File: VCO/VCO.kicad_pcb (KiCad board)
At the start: 2 copper layers, 45 parts, among them J1 Input, J2 Power, J3 Output, J4 PW, Q1 BC807, Q2 BC807, Q3 BC807, U1 LM324A, U2 LM324A

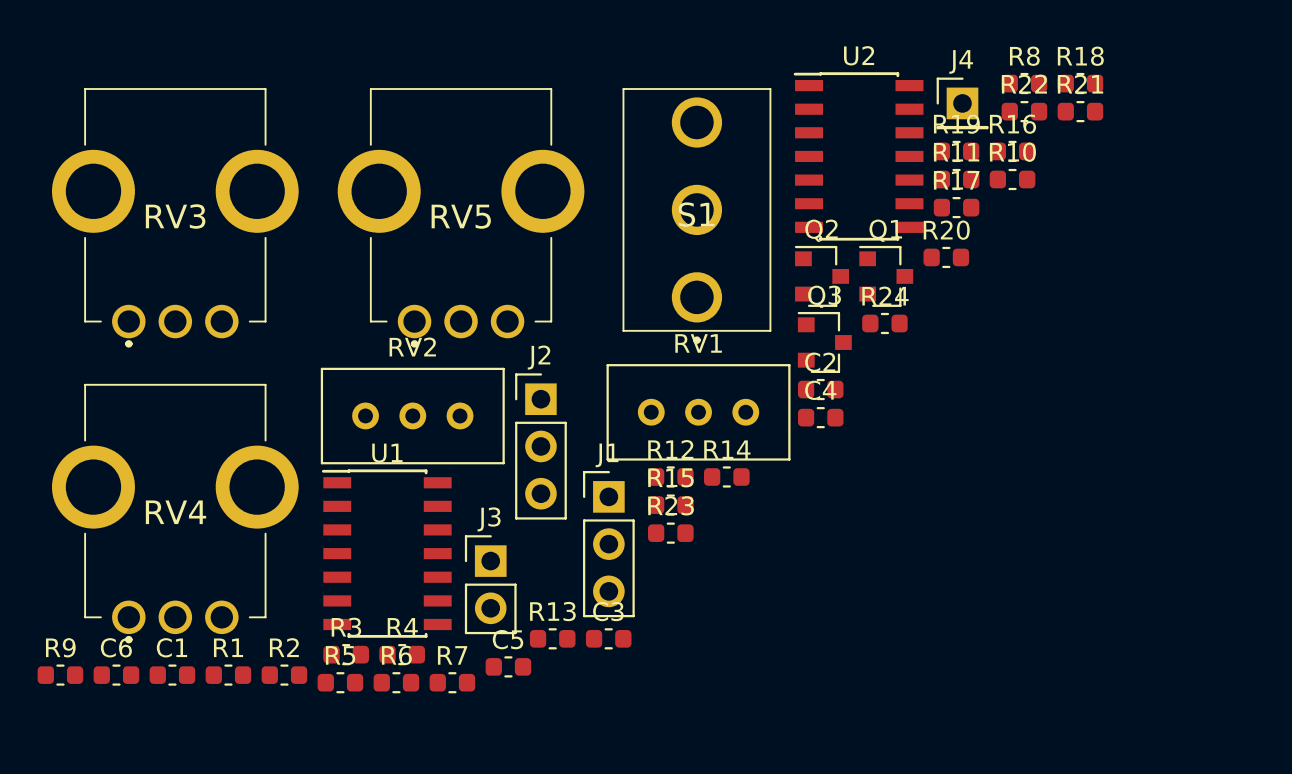
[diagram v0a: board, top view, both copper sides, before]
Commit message: Изменены библиотеки. Добавлинны библиотеки примененные в проекте локально. Добавленны заготовки для печатных плат. Добавленны 3D модели компоненток.
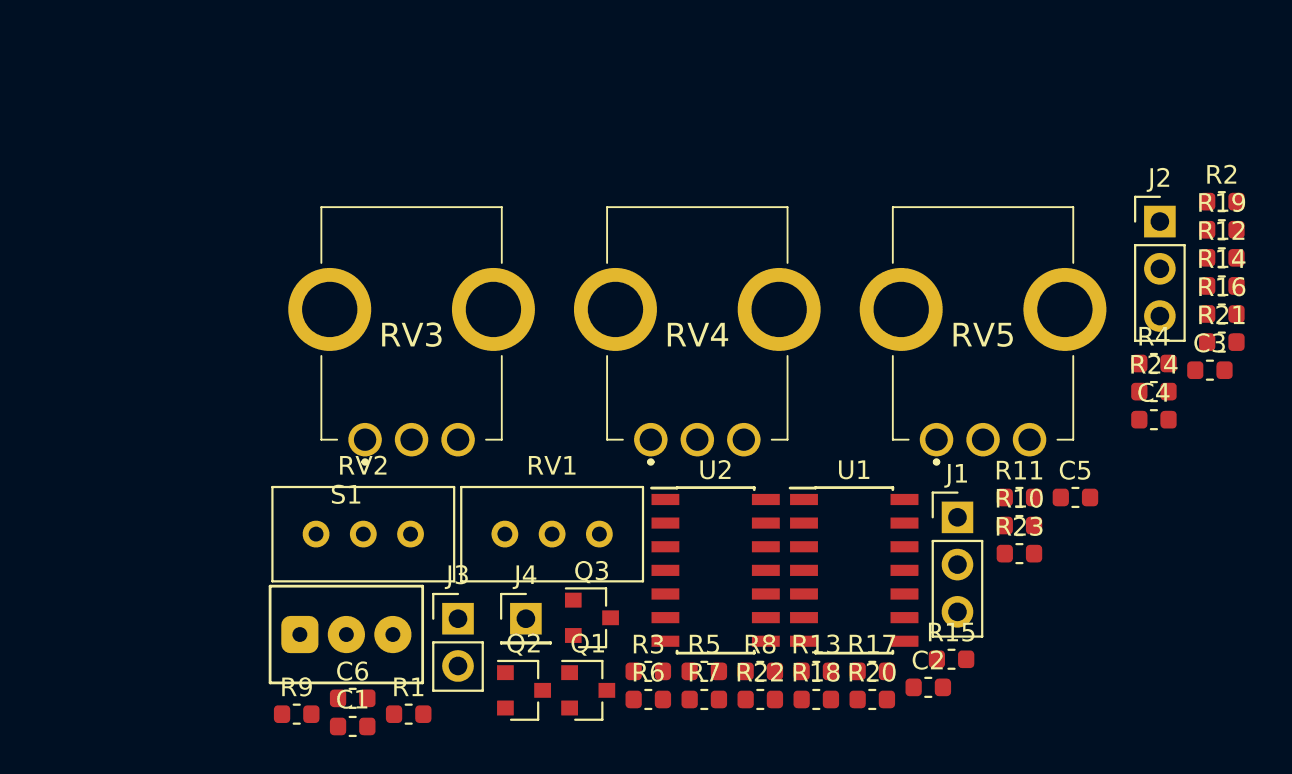
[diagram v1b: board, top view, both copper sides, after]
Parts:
- C1, C2, C3, C4, C5, C6: footprint Capacitor_SMD:C_0603_1608Metric -> footprint:c0603
- J1, J2: footprint Connector_PinHeader_2.54mm:PinHeader_1x03_P2.54mm_Vertical -> footprint:pls1x03
- J3: footprint Connector_PinHeader_2.54mm:PinHeader_1x02_P2.54mm_Vertical -> footprint:pls1x02
- J4: footprint Connector_PinHeader_2.54mm:PinHeader_1x01_P2.54mm_Vertical -> footprint:pls1x01
- Q1, Q2, Q3: footprint Package_TO_SOT_SMD:SOT-23 -> footprint:SOT-23
- R1, R10, R11, R12, R13, R14, R15, R16, R17, R18, R19, R2, R20, R21, R22, R23, R24, R3, R4, R5, R6, R7, R8, R9: footprint Resistor_SMD:R_0603_1608Metric -> footprint:r0603
- RV1, RV2: footprint Potentiometer_THT:Potentiometer_Bourns_3296W_Vertical -> footprint:w3296w
- RV3, RV4, RV5: footprint R0409N:PTV09A4020FB103 -> footprint:PTV09A4020FB103
- S1: footprint M2013SS1W03:M2018SD3G03 -> footprint:smts-102-2a2
- U1, U2: footprint Package_SO:SOIC-14_3.9x8.7mm_P1.27mm -> footprint:soic-14
- moved R2 56.5 mm to (178.2, 71.9)
- moved R4 43.3 mm to (174.6, 80.6)
- moved J4 36.3 mm to (140.8, 94.3)
- moved R18 36.0 mm to (156.4, 98.6)
- moved C3 35.4 mm to (177.6, 80.9)
- moved R22 34.6 mm to (153.4, 98.6)
- moved R8 34.6 mm to (153.4, 97.1)
- moved J2 34.6 mm to (174.9, 72.9)
- moved R12 31.9 mm to (178.2, 74.9)
- moved C5 31.8 mm to (170.4, 87.8)
- moved RV4 29.6 mm to (150.0, 79.1)
- moved S1 29.6 mm to (131.2, 95.1)
- moved RV5 28.8 mm to (165.4, 79.1)
- moved R14 28.5 mm to (178.2, 76.4)
- moved Q2 27.4 mm to (140.7, 98.1)
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
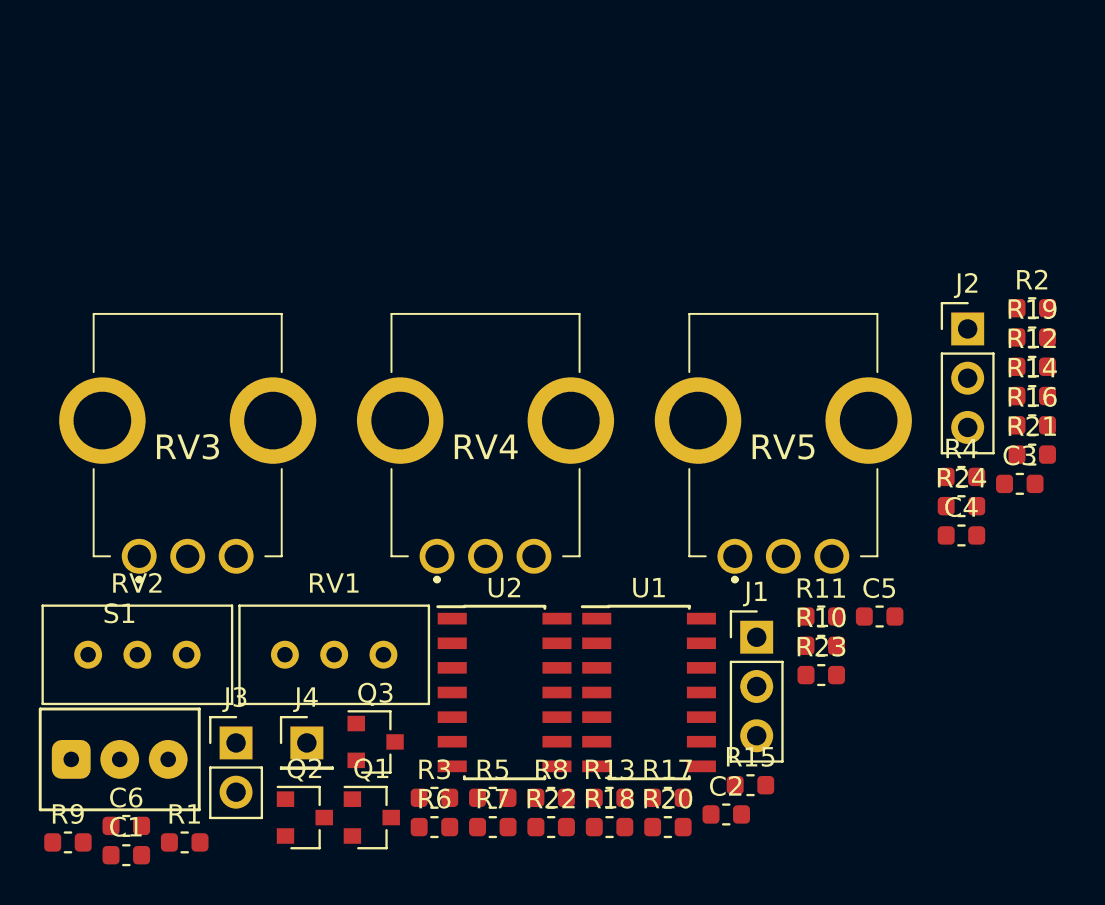
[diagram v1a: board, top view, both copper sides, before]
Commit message: Исправленну ошибки в схемах. Полностью локальные библиотеки и 3D модели.
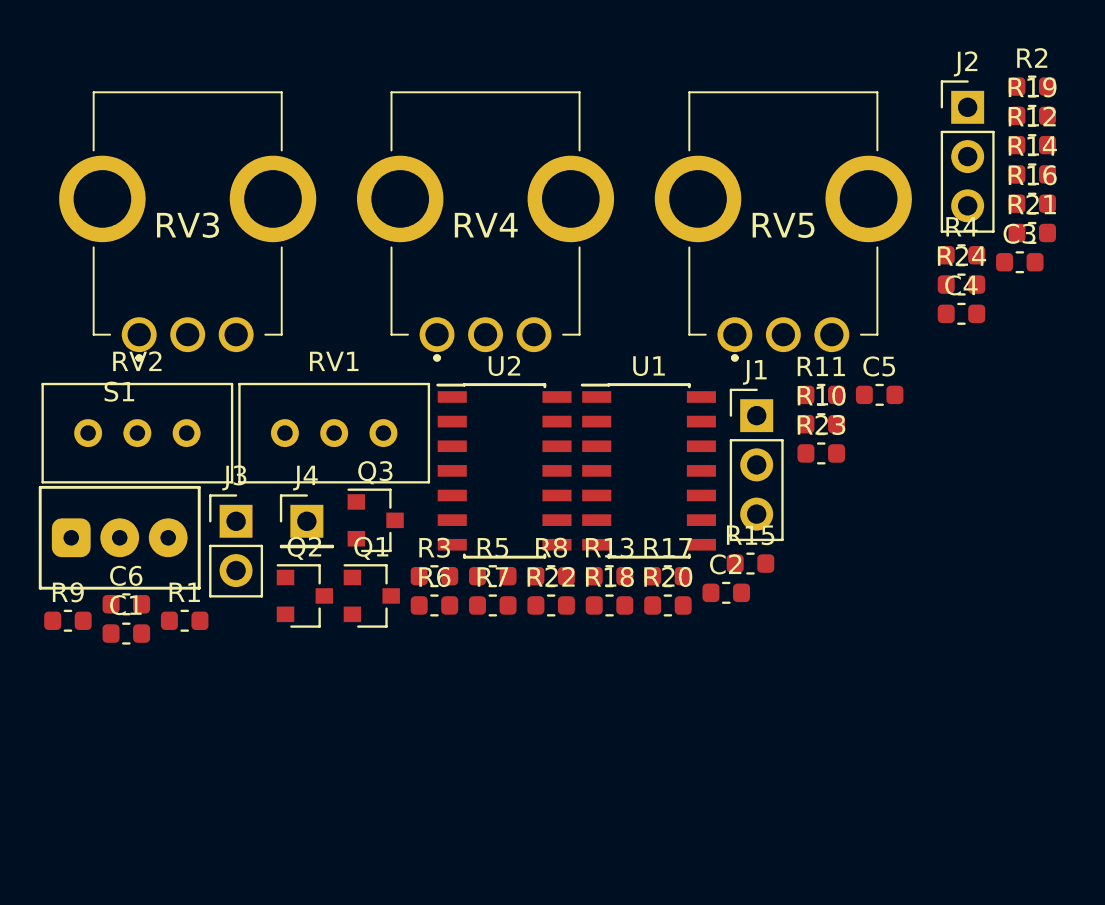
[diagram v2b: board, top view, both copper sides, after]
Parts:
- S1: footprint footprint:smts-102-2a2 -> footprint:smts
- moved C1 11.4 mm to (131.5, 88.7)
- moved C3 11.4 mm to (177.6, 69.5)
- moved C5 11.4 mm to (170.4, 76.3)
- moved C6 11.4 mm to (131.5, 87.1)
- moved J2 11.4 mm to (174.9, 61.5)
- moved Q3 11.4 mm to (144.4, 82.8)
- moved R11 11.4 mm to (167.4, 76.3)
- moved R15 11.4 mm to (163.7, 85.0)
- moved R16 11.4 mm to (178.2, 66.5)
- moved R18 11.4 mm to (156.4, 87.2)
- moved R20 11.4 mm to (159.4, 87.2)
- moved R22 11.4 mm to (153.4, 87.2)
- moved R24 11.4 mm to (174.6, 70.7)
- moved R4 11.4 mm to (174.6, 69.1)
- moved R6 11.4 mm to (147.4, 87.2)
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
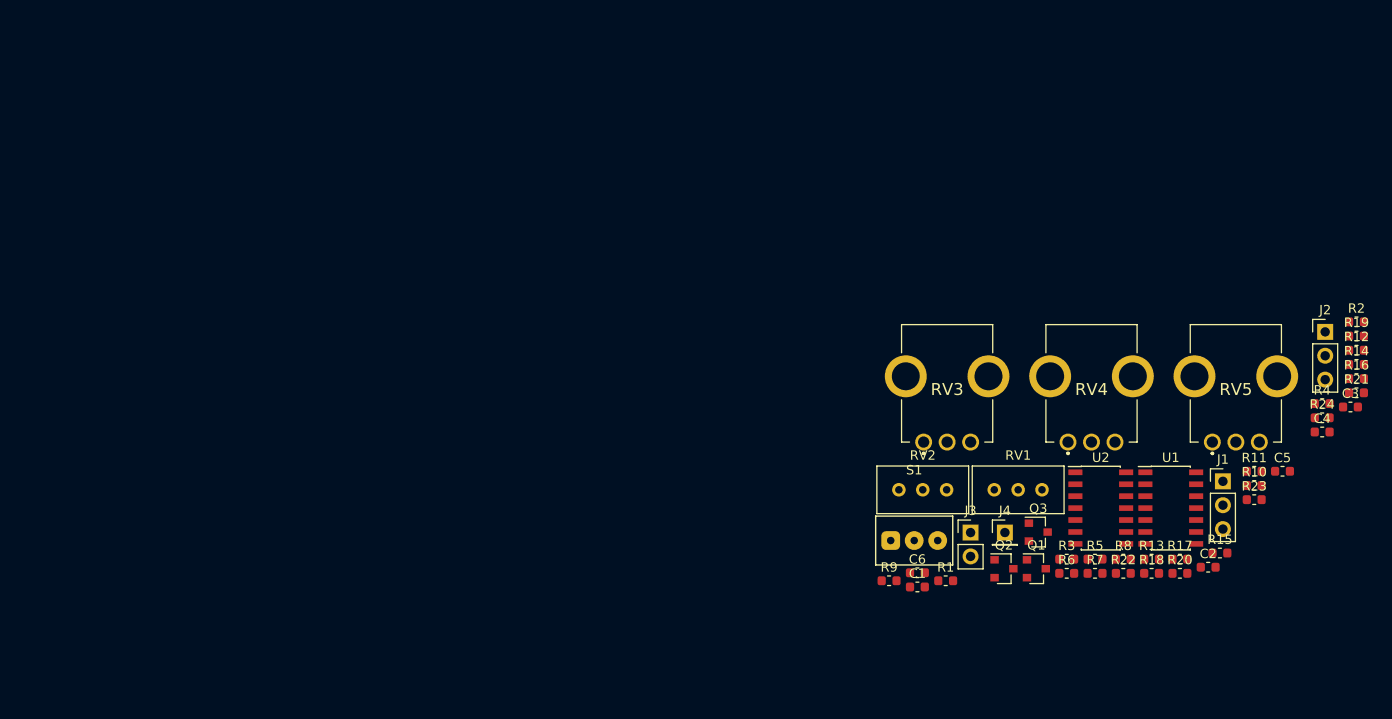
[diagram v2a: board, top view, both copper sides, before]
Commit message: ADD PCB module VCO. ADD folder MOTHEBORD.
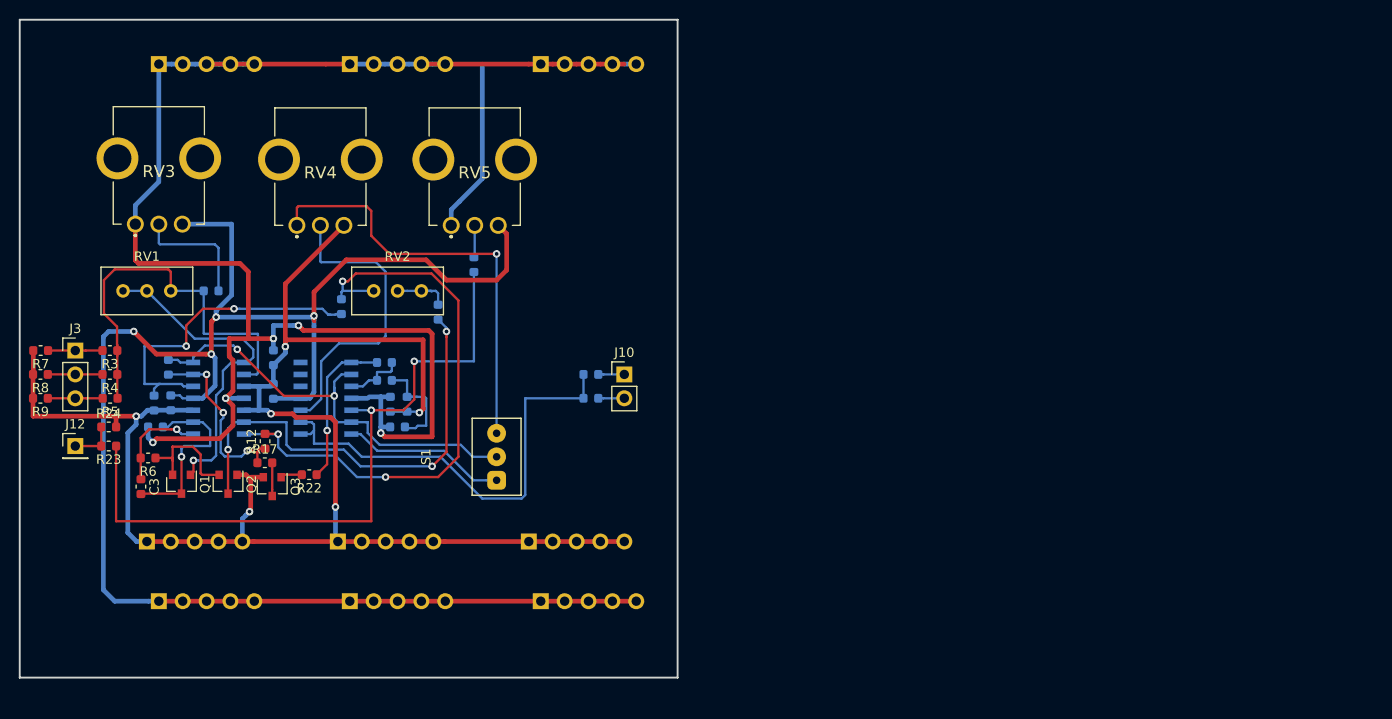
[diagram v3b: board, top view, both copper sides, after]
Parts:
- added J10: Output, footprint:pls1x02, F.Cu at (100.3, 66.0)
- added J11: Conn_01x05_Male, footprint:pls1x05, B.Cu at (91.4, 90.2)
- added J12: PW, footprint:pls1x01, F.Cu at (41.9, 73.7)
- added J5: Conn_01x05_Male, footprint:pls1x05, B.Cu at (49.5, 83.8)
- added J6: Conn_01x05_Male, footprint:pls1x05, B.Cu at (69.8, 83.8)
- added J7: Conn_01x05_Male, footprint:pls1x05, B.Cu at (90.2, 83.8)
- added J8: Conn_01x05_Male, footprint:pls1x05, B.Cu at (50.8, 90.2)
- added J9: Conn_01x05_Male, footprint:pls1x05, B.Cu at (71.1, 90.2)
- C1, C2, C4, C5, C6, R1, R10, R11, R13, R14, R15, R16, R18, R19, R2, R20, R21, U1, U2: moved to B.Cu
- J1: value Input -> Conn_01x05_Male; footprint footprint:pls1x03 -> footprint:pls1x05; moved to B.Cu
- J2: value Power -> Conn_01x05_Male; footprint footprint:pls1x03 -> footprint:pls1x05; moved to B.Cu
- J3: value Output -> Input; footprint footprint:pls1x02 -> footprint:pls1x03
- J4: value PW -> Conn_01x05_Male; footprint footprint:pls1x01 -> footprint:pls1x05; moved to B.Cu
- moved R24 129.1 mm to (45.5, 71.6)
- moved R4 129.0 mm to (45.6, 66.0), turned to 180 degrees
- moved C3 129.0 mm to (48.9, 78.0), turned to 270 degrees
- moved R23 122.0 mm to (45.5, 73.7), turned to 180 degrees
- moved C5 118.5 mm to (52.1, 69.1), turned to 270 degrees
- moved R8 116.9 mm to (38.2, 66.0), turned to 180 degrees
- moved R12 116.5 mm to (62.1, 73.2), turned to 90 degrees
- moved R7 114.7 mm to (38.2, 63.5), turned to 180 degrees
- moved R15 114.5 mm to (50.3, 69.1), turned to 270 degrees
- moved R10 112.9 mm to (56.4, 57.1)
- moved C4 111.7 mm to (63.0, 67.8), turned to 90 degrees
- moved R14 108.2 mm to (70.2, 58.8), turned to 90 degrees
- moved R5 106.2 mm to (45.6, 68.6), turned to 180 degrees
- moved R3 104.2 mm to (45.6, 63.5), turned to 180 degrees
- moved R19 103.5 mm to (74.8, 64.8)
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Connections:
- J1 pad 1: /IN_1 -> +5V
- J1 pad 2: /IN_2 -> +5V
- J1 pad 3: /IN_3 -> +5V
- J2 pad 2: GNDREF -> +5V
- J2 pad 3: -5V -> +5V
- J3 pad 1: Net-(J3-Pad1) -> /IN_1
- J3 pad 2: Net-(J3-Pad2) -> /IN_2
- J4 pad 1: /PW -> +5V
- R11 pad 1: Net-(J3-Pad1) -> Net-(J10-Pad1)
- R13 pad 1: Net-(J3-Pad2) -> Net-(J10-Pad2)
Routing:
- net +5V: track 0.00 -> 225.1 mm, vias 0 -> 5
- net -5V: track 0.00 -> 217.5 mm, vias 0 -> 4
- net GNDREF: track 0.00 -> 210.6 mm, vias 0 -> 6
- net Net-(R21-Pad1): track 0.00 -> 74.0 mm, vias 0 -> 2
- net Net-(R12-Pad2): track 0.00 -> 64.4 mm, vias 0 -> 3
- net Net-(R11-Pad2): track 0.00 -> 49.2 mm
- net Net-(Q2-Pad3): track 0.00 -> 48.9 mm, vias 0 -> 3
- net Net-(C6-Pad1): track 0.00 -> 47.6 mm, vias 0 -> 2
- net Net-(RV4-Pad1): track 0.00 -> 46.1 mm, vias 0 -> 1
- net Net-(R10-Pad1): track 0.00 -> 42.4 mm
- net Net-(R14-Pad1): track 0.00 -> 35.3 mm, vias 0 -> 2
- net Net-(Q1-Pad1): track 0.00 -> 34.7 mm, vias 0 -> 1
- net Net-(RV4-Pad2): track 0.00 -> 32.8 mm
- net Net-(C6-Pad2): track 0.00 -> 19.8 mm, vias 0 -> 3
- net Net-(C3-Pad2): track 0.00 -> 19.6 mm, vias 0 -> 1
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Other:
- board outline added: 70 x 70 mm
- net class power added: clearance 0.2, trace_width 0.5, via_dia 0.8, via_drill 0.4

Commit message: Изменение в схемах. Разведенны ПП
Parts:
- moved J11 3.83 mm to (91.4, 94.0)
- moved J8 3.83 mm to (50.8, 94.0)
- moved J9 3.83 mm to (71.1, 94.0)
- moved J5 3.18 mm to (49.5, 87.0)
- moved J6 3.18 mm to (69.8, 87.0)
- moved J7 3.18 mm to (90.2, 87.0)
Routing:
- net GNDREF: track 210.6 -> 220.6 mm
- net -5V: track 217.5 -> 221.3 mm
